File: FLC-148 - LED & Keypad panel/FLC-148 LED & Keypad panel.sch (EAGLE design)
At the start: 76 parts, among them IC1 MAX6818, IC2 MAX6818, IC3 NTGD3148NT1G, IC4 NTGD3148NT1G, IC5 STM32G071CBU6, IC6 ECS-480-10-33B-CKM-TR, J1 FTSH-107-01-L-DV-K-A

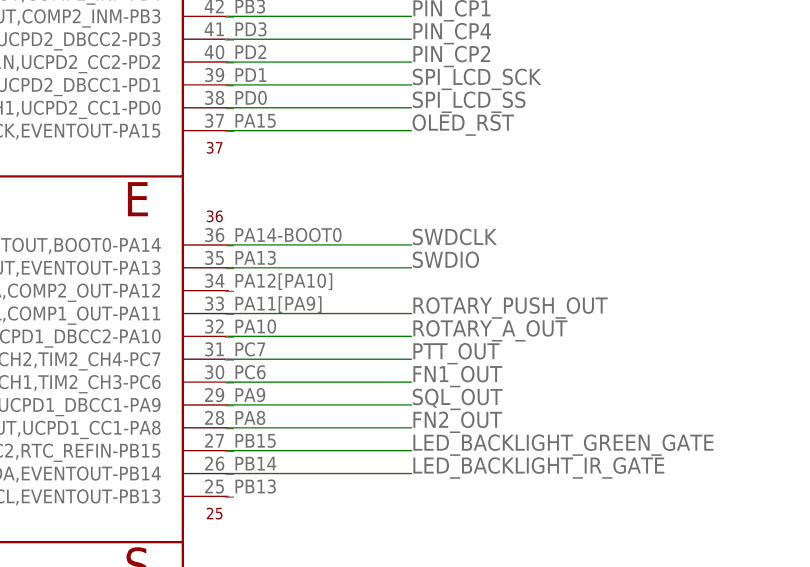
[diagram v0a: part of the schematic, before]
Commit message: - routed missing LCD D/C pin to PA12
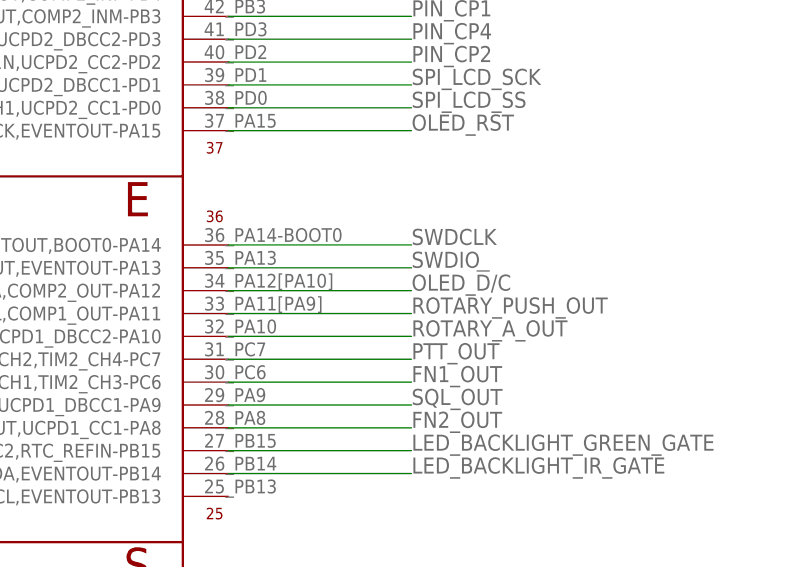
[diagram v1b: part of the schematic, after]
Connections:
- net OLED_!D!/C: now also IC5.SPI1_MOSI/I2S1_SD,USART1_RTS_DE_CK,TIM1_ETR,I2S_CKIN,I2C2_SDA,COMP2_OUT-PA12
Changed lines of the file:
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@@
 <label x="48.26" y="-7.62" size="1.778" layer="95"/>
+</segment>
+<segment>
+<pinref part="IC5" gate="G$1" pin="SPI1_MOSI/I2S1_SD,USART1_RTS_DE_CK,TIM1_ETR,I2S_CKIN,I2C2_SDA,COMP2_OUT-PA12"/>
+<wire x1="655.32" y1="-27.94" x2="675.64" y2="-27.94" width="0.1524" layer="91"/>
+<label x="675.64" y="-27.94" size="1.778" layer="95"/>
 </segment>
 </net>

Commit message: - renamed signals to be more consistent
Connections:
- net BACKLIGHT_GREEN_DRAIN renamed LCD_BACKLIGHT_GREEN_DRAIN
- net BACKLIGHT_IR_DRAIN renamed LCD_BACKLIGHT_IR_DRAIN
- net KEYPAD_IR_LED_DRAIN renamed KEYPAD_BACKLIGHT_IR_DRAIN
- net LED_BACKLIGHT_GREEN_GATE renamed OLED_BACKLIGHT_GREEN_GATE
- net LED_BACKLIGHT_IR_GATE renamed OLED_BACKLIGHT_IR_GATE
- net SPI_LCD_MOSI renamed SPI_OLED_MOSI
- net SPI_LCD_SCK renamed SPI_OLED_SCK
- net SPI_LCD_SS renamed SPI_OLED_SS
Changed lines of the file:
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@@
 </segment>
 </net>
-<net name="SPI_LCD_SCK" class="2">
+<net name="SPI_OLED_SCK" class="2">
 <segment>
 <pinref part="LCD" gate="G$1" pin="DB6_19"/>
@@
 </segment>
 </net>
-<net name="SPI_LCD_MOSI" class="2">
+<net name="SPI_OLED_MOSI" class="2">
 <segment>
 <pinref part="LCD" gate="G$1" pin="DB7_18"/>
@@
 </segment>
 </net>
-<net name="SPI_LCD_SS" class="2">
+<net name="SPI_OLED_SS" class="2">
 <segment>
 <pinref part="LCD" gate="G$1" pin="!CS1!_30"/>
@@
 </segment>
 </net>
-<net name="LED_BACKLIGHT_GREEN_GATE" class="2">
+<net name="OLED_BACKLIGHT_GREEN_GATE" class="2">
 <segment>
 <pinref part="IC5" gate="G$1" pin="SPI2_MOSI,TIM1_CH3N,TIM15_CH1N,TIM15_CH2,EVENTOUT,UCPD1_CC2,RTC_REFIN-PB15"/>
@@
 </segment>
 </net>
-<net name="LED_BACKLIGHT_IR_GATE" class="2">
+<net name="OLED_BACKLIGHT_IR_GATE" class="2">
 <segment>
 <pinref part="IC5" gate="G$1" pin="SPI2_MISO,UCPD1_FRSTX,TIM1_CH2N,USART3_RTS_DE_CK,TIM15_CH1,I2C2_SDA,EVENTOUT-PB14"/>
@@
 </segment>
 </net>
-<net name="BACKLIGHT_GREEN_DRAIN" class="2">
+<net name="LCD_BACKLIGHT_GREEN_DRAIN" class="2">
 <segment>
 <pinref part="IC3" gate="G$1" pin="6_D1"/>
@@
 </segment>
 </net>
-<net name="BACKLIGHT_IR_DRAIN" class="2">
+<net name="LCD_BACKLIGHT_IR_DRAIN" class="2">
 <segment>
 <pinref part="IC3" gate="G$1" pin="4_D2"/>
@@
 </segment>
 </net>
-<net name="KEYPAD_IR_LED_DRAIN" class="2">
+<net name="KEYPAD_BACKLIGHT_IR_DRAIN" class="2">
 <segment>
 <pinref part="LED5" gate="G$1" pin="C"/>

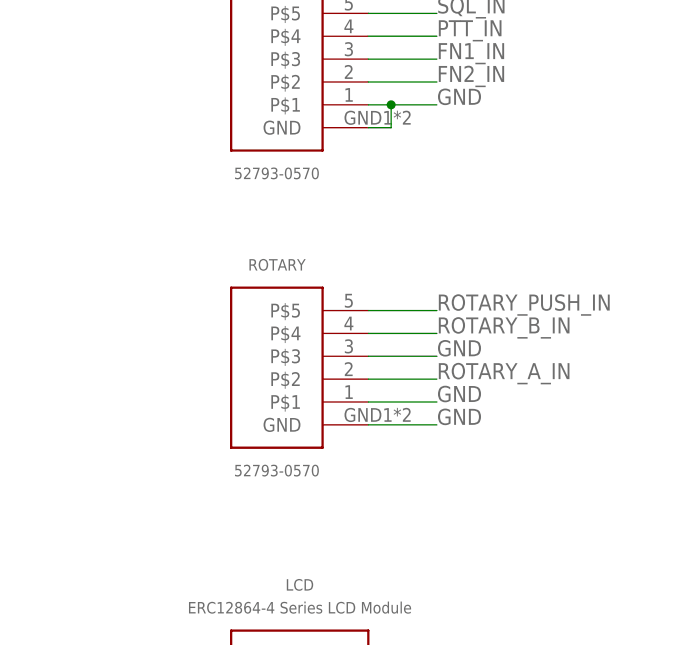
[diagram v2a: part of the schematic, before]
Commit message: - replaced 1mm 5p zif connector (52793-0570) with better part (52207-0533)
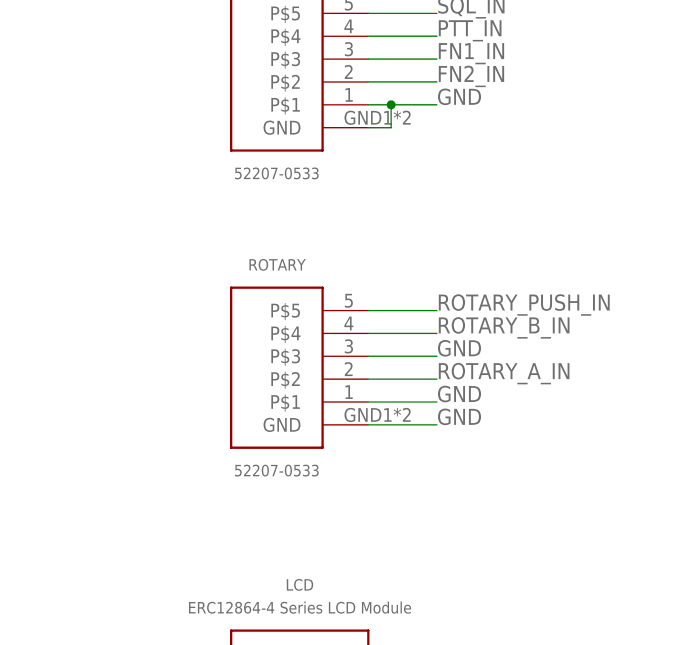
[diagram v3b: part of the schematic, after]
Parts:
- PTT, ROTARY: value 52793-0570 -> 52207-0533
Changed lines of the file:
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@@
 <part name="R2" library="741X163103JP 10k Ohm Resistor Array" deviceset="741X163" device="" value="741X163103JP - 10K"/>
 <part name="R3" library="741X163103JP 10k Ohm Resistor Array" deviceset="741X163" device="" value="741X163103JP - 10K"/>
-<part name="PTT" library="527930570 FFC Connector 5p 1mm Pitch" deviceset="527930570" device="" value="52793-0570"/>
+<part name="PTT" library="527930570 FFC Connector 5p 1mm Pitch" deviceset="527930570" device="" value="52207-0533"/>
 <part name="R4" library="741X163103JP 10k Ohm Resistor Array" deviceset="741X163" device="" value="EXB-2HV680JV  - 68 Ohm"/>
 <part name="IMIC" library="2-Pole Connector" deviceset="2POLE_CONNECTOR" device="" value="IMIC"/>
@@
 <part name="C19" library="rcl" library_urn="urn:adsk.eagle:library:334" deviceset="CPOL-EU" device="SMCA" package3d_urn="urn:adsk.eagle:package:25926/3" value="0.1μF Tantalum"/>
 <part name="C17" library="rcl" library_urn="urn:adsk.eagle:library:334" deviceset="CPOL-EU" device="SMCA" package3d_urn="urn:adsk.eagle:package:25926/3" value="4.7μF Tantalum"/>
-<part name="ROTARY" library="527930570 FFC Connector 5p 1mm Pitch" deviceset="527930570" device="" value="52793-0570"/>
+<part name="ROTARY" library="527930570 FFC Connector 5p 1mm Pitch" deviceset="527930570" device="" value="52207-0533"/>
 <part name="MCU" library="5034801800 FFC Connector 19p 0.5mm Pitch, FLC148 Motherboard - LCD Panel" deviceset="5034801800-MOTHERBOARD&lt;-&gt;LCD-PANEL" device="" value="503480-1800"/>
 <part name="C10" library="rcl" library_urn="urn:adsk.eagle:library:334" deviceset="C-EU" device="C0402" package3d_urn="urn:adsk.eagle:package:23626/2" value="1μF"/>

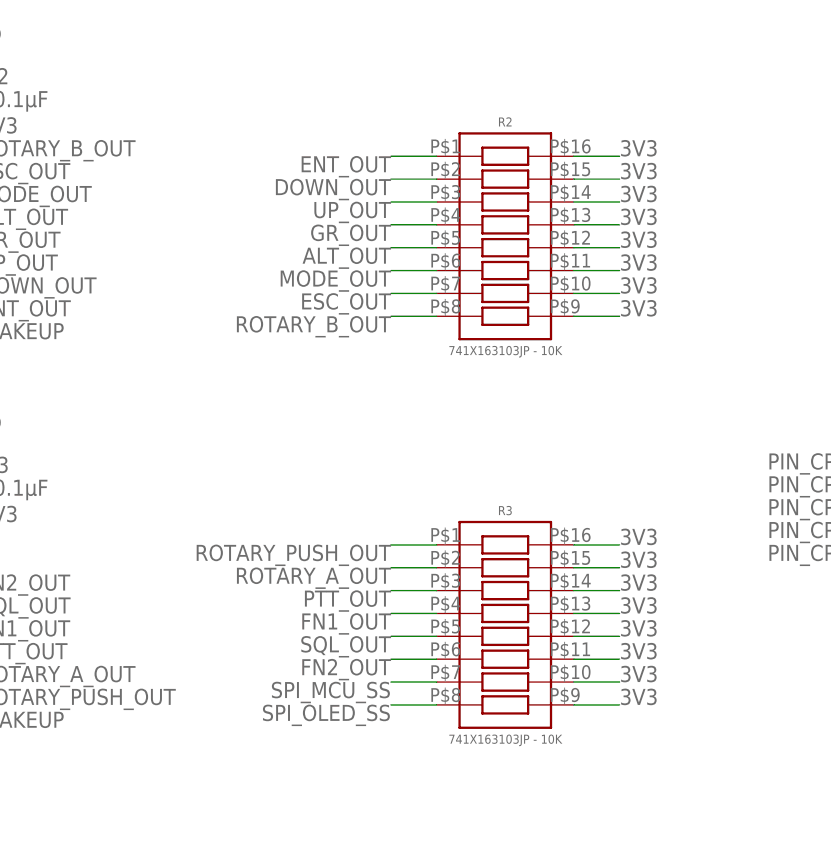
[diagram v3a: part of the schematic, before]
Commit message: - started to remove 10k resistor arrays since pullups in the stm32 can replace them
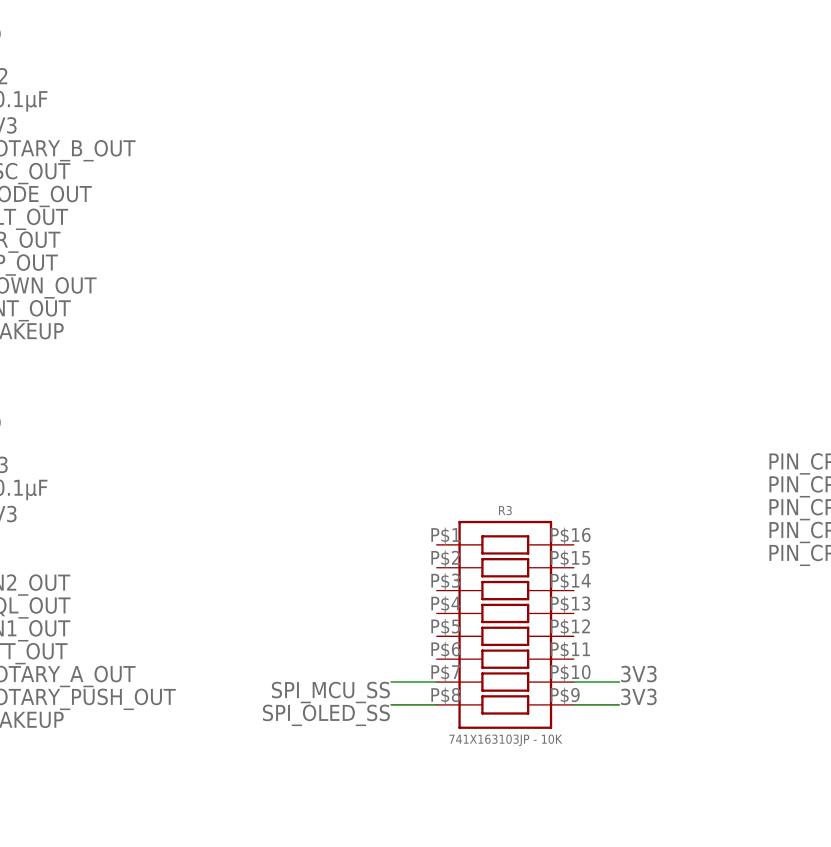
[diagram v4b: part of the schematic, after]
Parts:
- removed R2: 741X163103JP - 10K, 741X163103JP 10k Ohm Resistor Array:741X163
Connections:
- net 3V3: no longer R2.P$10, R2.P$11, R2.P$12, R2.P$13, R2.P$14, R2.P$15, R2.P$16, R2.P$9, R3.P$11, R3.P$12, R3.P$13, R3.P$14, R3.P$15, R3.P$16
- net ALT_OUT: no longer R2.P$5
- net DOWN_OUT: no longer R2.P$2
- net ENT_OUT: no longer R2.P$1
- net ESC_OUT: no longer R2.P$7
- net FN1_OUT: no longer R3.P$4
- net FN2_OUT: no longer R3.P$6
- net GR_OUT: no longer R2.P$4
- net MODE_OUT: no longer R2.P$6
- net PTT_OUT: no longer R3.P$3
- net ROTARY_A_OUT: no longer R3.P$2
- net ROTARY_B_OUT: no longer R2.P$8
- net ROTARY_PUSH_OUT: no longer R3.P$1
- net SQL_OUT: no longer R3.P$5
- net UP_OUT: no longer R2.P$3

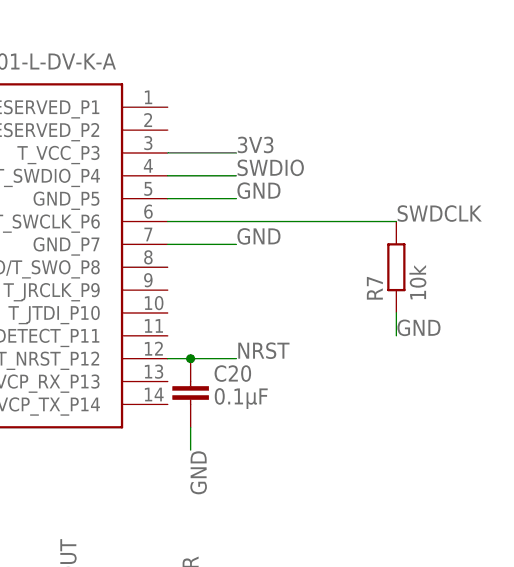
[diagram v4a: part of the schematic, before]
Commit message: - removed R7 (swdclk to gnd), since it is not needed
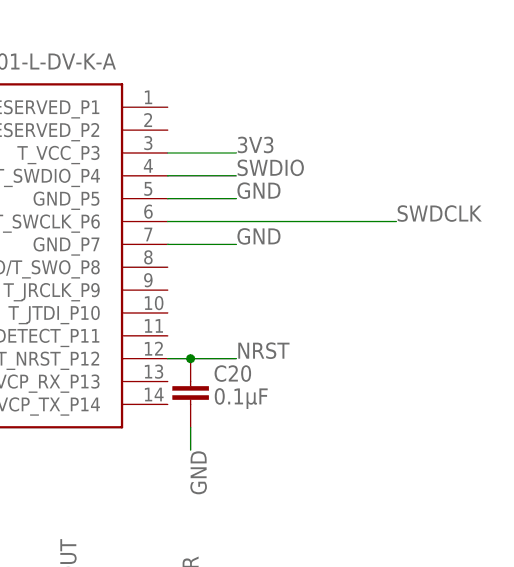
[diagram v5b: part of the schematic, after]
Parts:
- removed R7: 10k, rcl:R-EU_R0402
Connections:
- net GND: no longer R7.1
- net SWDCLK: no longer R7.2
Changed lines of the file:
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@@
 <part name="IC6" library="ECS-480-10-33B-CKM-TR 48MHz Crystal" deviceset="ECS-480-10-33B-CKM-TR" device="" value="ECS-480-10-33B-CKM-TR"/>
 <part name="C20" library="rcl" library_urn="urn:adsk.eagle:library:334" deviceset="C-EU" device="C0402" package3d_urn="urn:adsk.eagle:package:23626/2" value="0.1μF"/>
-<part name="R7" library="rcl" library_urn="urn:adsk.eagle:library:334" deviceset="R-EU_" device="R0402" package3d_urn="urn:adsk.eagle:package:23547/3" value="10k"/>
 <part name="R8" library="rcl" library_urn="urn:adsk.eagle:library:334" deviceset="R-EU_" device="R0402" package3d_urn="urn:adsk.eagle:package:23547/3" value="100k"/>
 <part name="R9" library="rcl" library_urn="urn:adsk.eagle:library:334" deviceset="R-EU_" device="R0402" package3d_urn="urn:adsk.eagle:package:23547/3" value="300k"/>
@@
 <attribute name="VALUE" x="784.86" y="-45.72" size="1.778" layer="96"/>
 </instance>
-<instance part="R7" gate="G$1" x="805.18" y="-30.48" smashed="yes" rot="R90">
-<attribute name="NAME" x="803.6814" y="-34.29" size="1.778" layer="95" rot="R90"/>
-<attribute name="VALUE" x="808.482" y="-34.29" size="1.778" layer="96" rot="R90"/>
-</instance>
 <instance part="R8" gate="G$1" x="167.64" y="-43.18" smashed="yes" rot="R90">
 <attribute name="NAME" x="166.1414" y="-46.99" size="1.778" layer="95" rot="R90"/>
@@
 <wire x1="782.32" y1="-48.26" x2="782.32" y2="-50.8" width="0.1524" layer="91"/>
 <label x="782.32" y="-50.8" size="1.778" layer="95" rot="R270"/>
-</segment>
-<segment>
-<pinref part="R7" gate="G$1" pin="1"/>
-<wire x1="805.18" y1="-35.56" x2="805.18" y2="-38.1" width="0.1524" layer="91"/>
-<label x="805.18" y="-38.1" size="1.778" layer="95"/>
 </segment>
 <segment>
@@
 <pinref part="J1" gate="G$1" pin="T_JCLK/T_SWCLK_P6"/>
 <label x="805.18" y="-25.4" size="1.778" layer="95"/>
-<pinref part="R7" gate="G$1" pin="2"/>
 <wire x1="779.78" y1="-25.4" x2="805.18" y2="-25.4" width="0.1524" layer="91"/>
 </segment>

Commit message: - connected rotary encoder A and B out directly to micro controller (previously these lines were going through the debouncing IC)
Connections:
- removed net ROTARY_A_OUT: IC2.OUT7, IC5.SPI2_MOSI,USART1_RX,TIM1_CH3,TIM17_BKIN,I2C1_SDA,EVENTOUT,UCPD1_DBCC2-PA10
- removed net ROTARY_B_OUT: IC1.OUT1, IC5.USART1_TX,TIM1_CH3,TIM16_CH1N,SPI2_MISO,LPTIM1_ETR,I2C1_SCL,EVENTOUT,COMP2_INP-PB6
- net ROTARY_A_IN: now also IC5.SPI2_MOSI,USART1_RX,TIM1_CH3,TIM17_BKIN,I2C1_SDA,EVENTOUT,UCPD1_DBCC2-PA10; no longer IC2.IN7
- net ROTARY_B_IN: now also IC5.USART1_TX,TIM1_CH3,TIM16_CH1N,SPI2_MISO,LPTIM1_ETR,I2C1_SCL,EVENTOUT,COMP2_INP-PB6; no longer IC1.IN1
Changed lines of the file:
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@@
-</segment>
-<segment>
-<pinref part="IC1" gate="G$1" pin="IN1"/>
-<wire x1="104.14" y1="111.76" x2="99.06" y2="111.76" width="0.1524" layer="91"/>
-<label x="99.06" y="111.76" size="1.778" layer="95" rot="R180"/>
-</segment>
-</net>
-<net name="ROTARY_A_OUT" class="2">
-<segment>
-<pinref part="IC2" gate="G$1" pin="OUT7"/>
-<wire x1="134.62" y1="53.34" x2="142.24" y2="53.34" width="0.1524" layer="91"/>
-<label x="142.24" y="53.34" size="1.778" layer="95"/>
-</segment>
-<segment>
-<pinref part="IC5" gate="G$1" pin="SPI2_MOSI,USART1_RX,TIM1_CH3,TIM17_BKIN,I2C1_SDA,EVENTOUT,UCPD1_DBCC2-PA10"/>
-<wire x1="655.32" y1="-33.02" x2="675.64" y2="-33.02" width="0.1524" layer="91"/>
-<label x="675.64" y="-33.02" size="1.778" layer="95"/>
-</segment>
-</net>
-<net name="ROTARY_B_OUT" class="2">
-<segment>
-<pinref part="IC1" gate="G$1" pin="OUT1"/>
-<wire x1="134.62" y1="111.76" x2="142.24" y2="111.76" width="0.1524" layer="91"/>
-<label x="142.24" y="111.76" size="1.778" layer="95"/>
 </segment>
 <segment>
@@
 </segment>
 <segment>
-<pinref part="IC2" gate="G$1" pin="IN7"/>
-<wire x1="104.14" y1="53.34" x2="99.06" y2="53.34" width="0.1524" layer="91"/>
-<label x="99.06" y="53.34" size="1.778" layer="95" rot="R180"/>
+<pinref part="IC5" gate="G$1" pin="SPI2_MOSI,USART1_RX,TIM1_CH3,TIM17_BKIN,I2C1_SDA,EVENTOUT,UCPD1_DBCC2-PA10"/>
+<wire x1="655.32" y1="-33.02" x2="675.64" y2="-33.02" width="0.1524" layer="91"/>
+<label x="675.64" y="-33.02" size="1.778" layer="95"/>
 </segment>
 </net>

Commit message: - added todo/pin annotations where needed
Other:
- note added: "GPIO (input)"
- note added: "GPIO (output)"
- note added: "PWM"
- note added: "PWM (output)"
- note added: "TODO - logic gates: add logic OR gates to pushbutton switches & tie to wakeup pin so that microcontroller can be waken up on key press - quad FET: replace 2 dual FETs with one quad fet component - output debouncing: add debouncing circuitry to rotary encoder A and B output channels - pulldown: add 10k pulldown to FET gate pins -"
- note added: "TODO: logic gates"
- note added: "TODO: output debouncing"
- note added: "TODO: pulldown"
- note added: "TODO: quad FET"
- note added: "WKUP1"
- note added: "WKUP2"
- note added: "WKUP4"
- note added: "WKUP6"
- note removed: "wakeup"
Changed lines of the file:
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@@
 <wire x1="833.12" y1="129.54" x2="833.12" y2="-218.44" width="0.1524" layer="90"/>
 <wire x1="833.12" y1="-218.44" x2="459.74" y2="-218.44" width="0.1524" layer="90"/>
-<text x="693.42" y="5.08" size="1.778" layer="97">SPI2 - master for LCD</text>
+<text x="706.12" y="5.08" size="1.778" layer="97">SPI2 - master for LCD</text>
 <text x="304.8" y="-2.54" size="1.778" layer="97" rot="R180">Itotal = 7*70mA = 490mA, Uf=1.4V
 Presistor = 490mA*1.4V=686mW</text>
 <text x="307.34" y="-124.46" size="1.778" layer="97" rot="R180">Itotal=4*50mA = 200mA, U =1.6V
 Presistor=0.2A*1.6V=0.32W</text>
-<text x="662.94" y="-129.54" size="1.778" layer="98">wakeup</text>
-<text x="662.94" y="-104.14" size="1.778" layer="98">wakeup</text>
-<text x="662.94" y="-91.44" size="1.778" layer="98">wakeup</text>
-<text x="662.94" y="7.62" size="1.778" layer="98">wakeup</text>
-<text x="685.8" y="-127" size="1.778" layer="98">TODO: tie boot0 to gnd</text>
+<text x="703.58" y="-129.54" size="1.778" layer="98">WKUP2</text>
+<text x="711.2" y="-104.14" size="1.778" layer="98">WKUP1</text>
+<text x="706.12" y="-91.44" size="1.778" layer="98">WKUP4</text>
+<text x="690.88" y="-22.86" size="1.778" layer="98">TODO: tie boot0 to gnd</text>
 <text x="132.08" y="-15.24" size="1.778" layer="90">BOOT0 pin</text>
+<text x="716.28" y="-45.72" size="1.778" layer="91">PWM (output)</text>
+<text x="701.04" y="-30.48" size="1.778" layer="91">GPIO (input)</text>
+<text x="713.74" y="-73.66" size="1.778" layer="91">PWM</text>
+<text x="693.42" y="-33.02" size="1.778" layer="91">GPIO (input)</text>
+<text x="688.34" y="-35.56" size="1.778" layer="91">GPIO (input)</text>
+<text x="688.34" y="-38.1" size="1.778" layer="91">GPIO (input)</text>
+<text x="688.34" y="-40.64" size="1.778" layer="91">GPIO (input)</text>
+<text x="688.34" y="-43.18" size="1.778" layer="91">GPIO (input)</text>
+<text x="690.88" y="-101.6" size="1.778" layer="91">GPIO (input)</text>
+<text x="688.34" y="-129.54" size="1.778" layer="91">GPIO (input)</text>
+<text x="688.34" y="-124.46" size="1.778" layer="91">GPIO (input)</text>
+<text x="688.34" y="-127" size="1.778" layer="91">GPIO (input)</text>
+<text x="690.88" y="17.78" size="1.778" layer="91">GPIO (input)</text>
+<text x="688.34" y="15.24" size="1.778" layer="91">GPIO (input)</text>
+<text x="688.34" y="7.62" size="1.778" layer="91">GPIO (output)</text>
+<text x="688.34" y="2.54" size="1.778" layer="91">GPIO (output)</text>
+<text x="688.34" y="0" size="1.778" layer="91">GPIO (output)</text>
+<text x="688.34" y="-2.54" size="1.778" layer="91">GPIO (output)</text>
+<text x="688.34" y="5.08" size="1.778" layer="91">GPIO (output)</text>
+<text x="690.88" y="-10.16" size="1.778" layer="91">GPIO (output)</text>
+<text x="690.88" y="-27.94" size="1.778" layer="91">GPIO (output)</text>
+<text x="693.42" y="10.16" size="1.778" layer="91">GPIO (input)</text>
+<text x="711.2" y="-48.26" size="1.778" layer="91">PWM (output)</text>
+<text x="688.34" y="-91.44" size="1.778" layer="91">GPIO (input)</text>
+<text x="347.98" y="-167.64" size="1.778" layer="94">TODO: quad FET</text>
+<text x="685.8" y="-104.14" size="1.9304" layer="94">TODO: logic gates</text>
+<text x="855.98" y="-25.4" size="1.778" layer="94" align="top-left">TODO
+- logic gates: add logic OR gates to pushbutton switches &amp; tie to wakeup pin so that microcontroller can be waken up on key press
+- quad FET: replace 2 dual FETs with one quad fet component
+- output debouncing: add debouncing circuitry to rotary encoder A and B output channels
+- pulldown: add 10k pulldown to FET gate pins
+- </text>
+<text x="55.88" y="33.02" size="1.778" layer="94">TODO: output debouncing</text>
+<text x="396.24" y="-175.26" size="1.778" layer="94">TODO: pulldown</text>
+<text x="398.78" y="-180.34" size="1.778" layer="94">TODO: pulldown</text>
+<text x="396.24" y="-200.66" size="1.778" layer="94">TODO: pulldown</text>
+<text x="706.12" y="7.62" size="1.778" layer="98">WKUP6</text>
 </plain>
 <instances>
